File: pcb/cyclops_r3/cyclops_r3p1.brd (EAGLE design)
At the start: 69.8 x 53.3 mm, 74 parts, among them Q1 SUM11006, Q2 IRF510, U1 MCP4921, U2 317-N, U3 ADR03, U4 OP1177, U5 LM324N, U6 ZXTD45, U8 TLV3701CDBVT

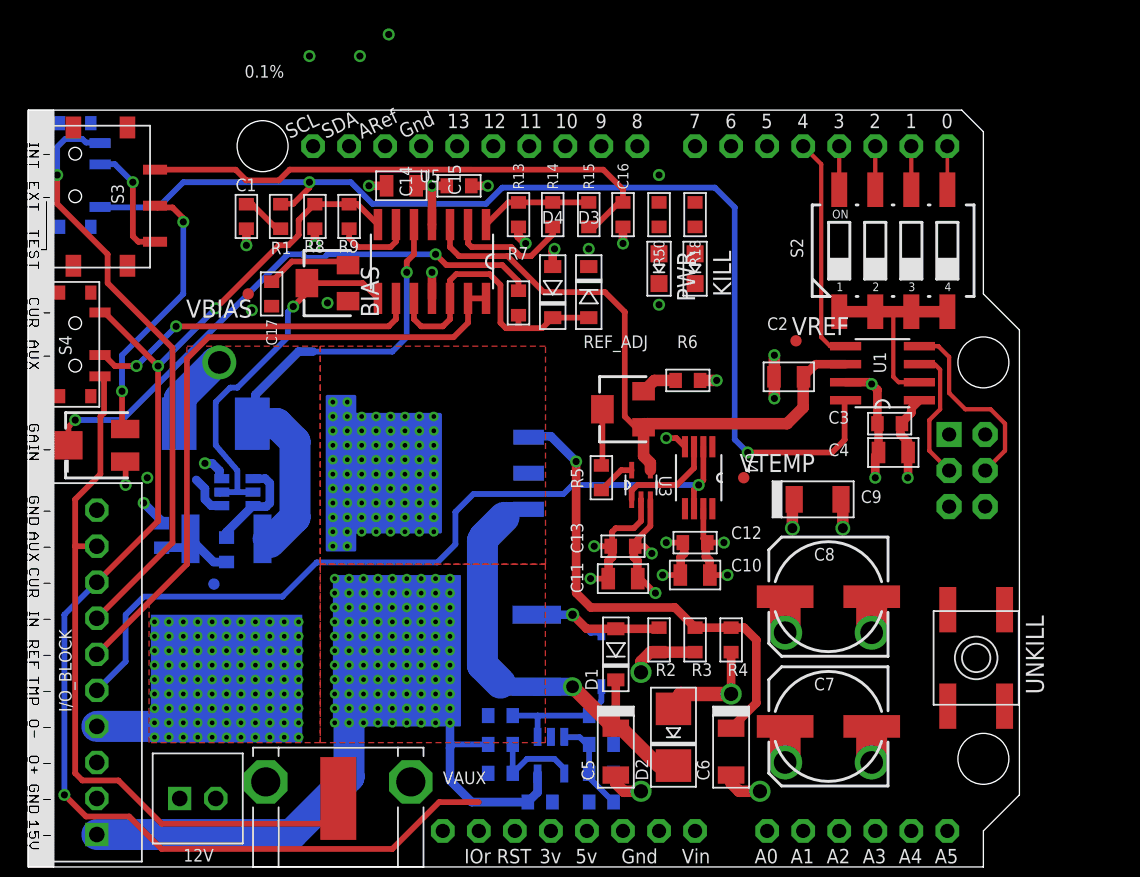
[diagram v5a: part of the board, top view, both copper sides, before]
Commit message: Several changes to board layout. Also, some new design notes.
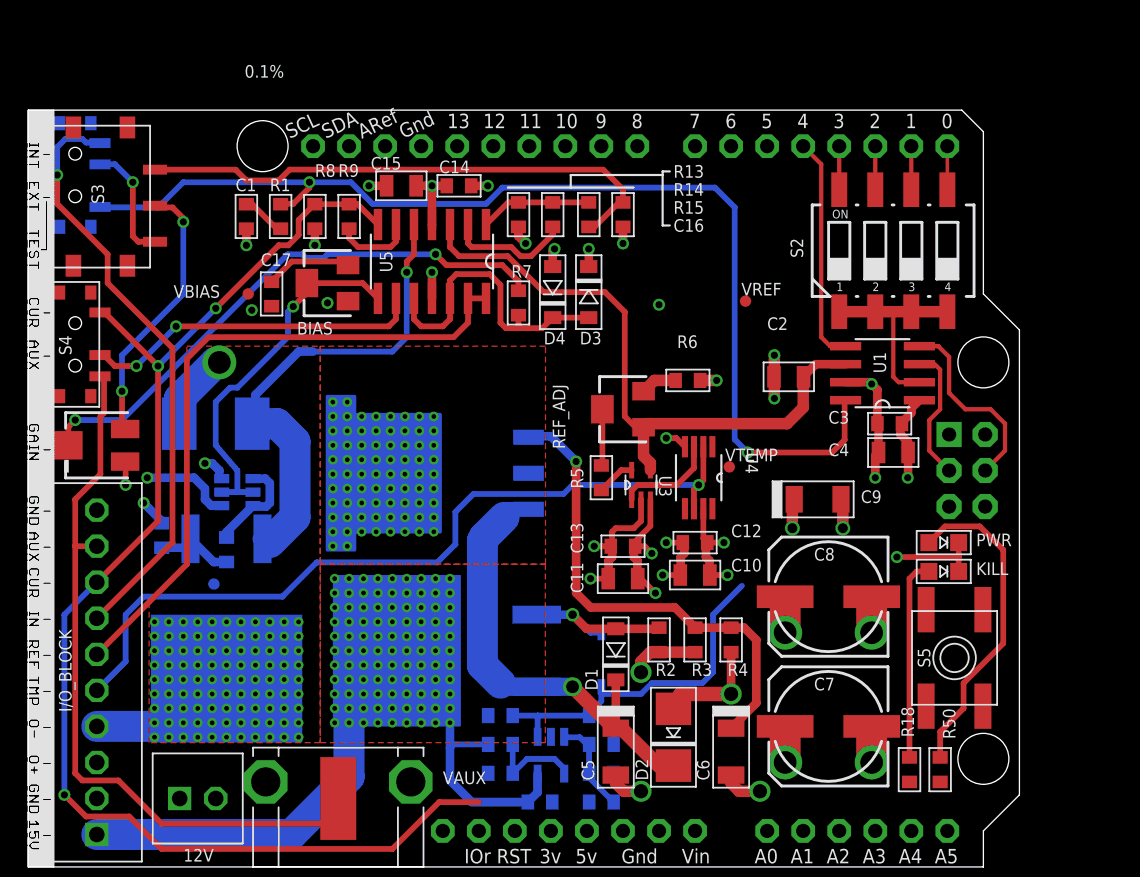
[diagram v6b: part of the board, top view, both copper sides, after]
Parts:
- removed UNKILL: SPST_TACT-EVQQ2, cyclops:EVQ-Q2
- added S5: UNKILL, cyclops:EVQ-Q2
- moved R50 43.8 mm to (63.0, 6.86), turned to 270 degrees
- moved R18 41.9 mm to (60.8, 6.86), turned to 270 degrees
- moved PWR 27.8 mm to (63.2, 22.9), turned to 270 degrees
- moved KILL 27.6 mm to (63.2, 20.8), turned to 270 degrees
- moved VREF 4.52 mm to (49.3, 39.9)
- moved VTEMP 1.27 mm to (48.1, 28.2)
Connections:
- removed net AGND: BIAS.3, C17.2, UNKILL.B, UNKILL.B'
- net COMP+: now also S5.A, S5.A'; no longer UNKILL.A, UNKILL.A'
- net GND: now also BIAS.3, C17.2, S5.B, S5.B'
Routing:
- net N$3: track 0.00 -> 22.9 mm
- net KILL: track 9.28 -> 24.7 mm
- net N$11: track 0.00 -> 14.2 mm
- net GND: track 68.7 -> 81.2 mm, vias 31 -> 30
- net AGND: track 6.08 -> 0.00 mm
- net +12V: track 40.5 -> 45.3 mm, vias 91 -> 89

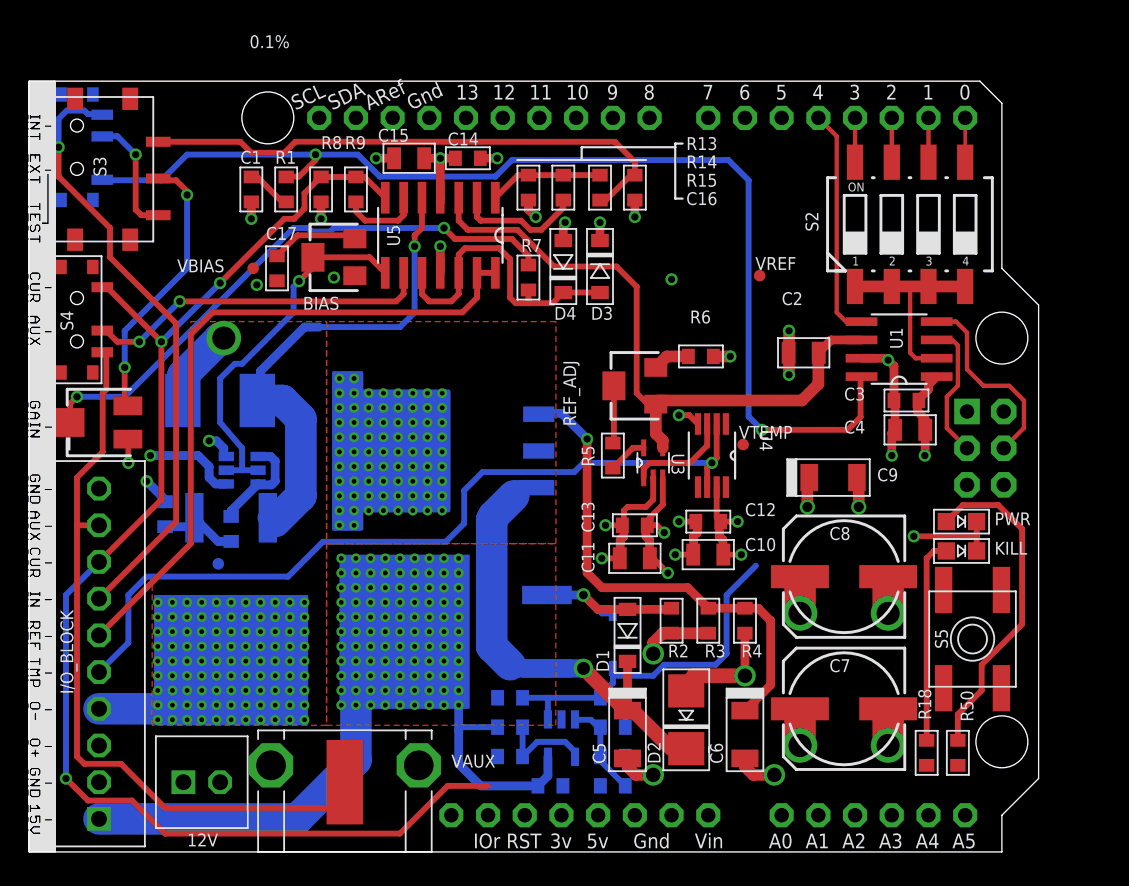
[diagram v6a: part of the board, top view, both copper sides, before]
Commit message: Added a negative rail, used exclusively by the opamp, to allow a wider bandwidth. Finished routing everything. Need to make bottom silkscreen and finish testing comparitor circuit.
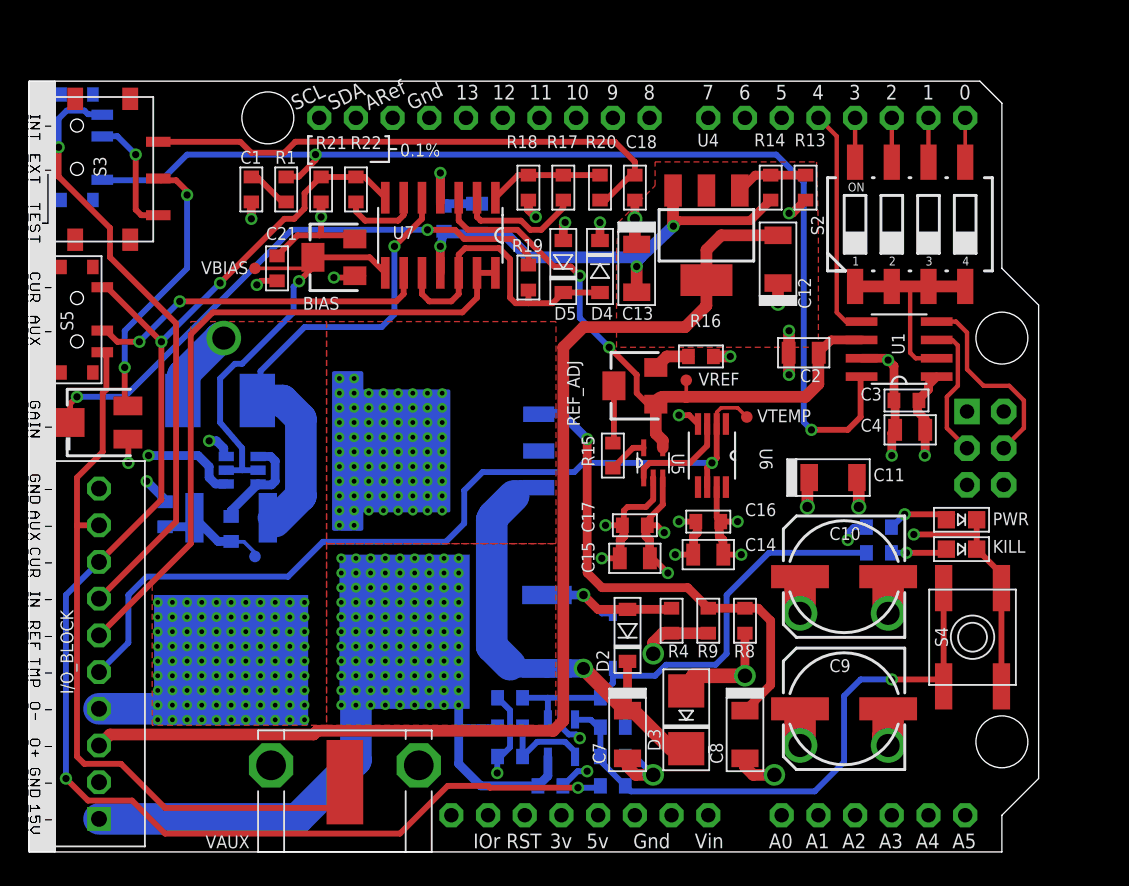
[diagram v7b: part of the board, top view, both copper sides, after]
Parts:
- removed 12V: SCREW2, cyclops:SCREW2
- removed R50: 2.4k, cyclops:0603
- added C20: 1uF, cyclops:0805
- added C21: .1uF, cyclops:0603
- added R22: 9k, cyclops:0603
- added R23: 10, cyclops:0603
- added R24: 1k, cyclops:0603
- added U7: LM324N, cyclops:SO14
- C10: value 1uF -> 47uF; device cyclops:0805 -> cyclops:153CLV-0807
- C11: device cyclops:0805 -> cyclops:1206-POL
- C12, C13: value .1uF -> 1uF; device cyclops:0603 -> cyclops:1206-POL
- C14: value .1uF -> 1uF; device cyclops:0603 -> cyclops:0805
- C19: value 10pF -> .1uF
- C5: value 1uF -> 10pF; device cyclops:1206-POL -> cyclops:0603
- C6: value 10uF -> .1uF; device cyclops:1206-POL -> cyclops:0603
- C7: value 47uF -> 1uF; device cyclops:153CLV-0807 -> cyclops:1206-POL
- C8: value 47uF -> 10uF; device cyclops:153CLV-0807 -> cyclops:1206-POL
- C9: value 1uF -> 47uF; device cyclops:1206-POL -> cyclops:153CLV-0807
- D1: value MMSZ -> (none); device cyclops:SOD123 -> cyclops:SOD-323F
- D2: value S1B -> MMSZ; device cyclops:SMA-DO214AC -> cyclops:SOD123
- D3: value DS11015 -> S1B; device cyclops:SOD123 -> cyclops:SMA-DO214AC
- D5: value (none) -> DS11015; device cyclops:SOD-323F -> cyclops:SOD123
- R10: value 10 -> 220k
- R11: value 220k -> 3.0k
- R12: value 1k -> 2.4k
- R13: value 1k -> 75
- R14: value 1k -> 120
- R15: value 1k -> 470
- R16: value 100k -> 1k
- R18: value 3.0k -> 1k
- R19: value 4k -> 1k
- R2: value 10k -> 100k
- R20: value 56k -> 1k
- R21: value 91k -> 1k
- R3: value 2.1k -> 56k
- R4: value 240 -> 10k
- R5: value 470 -> 4k
- R6: value 1k -> 91k
- R8: value 1k -> 240
- R9: value 9k -> 2.1k
- S4: value CURR/AUX -> UNKILL; device cyclops:PCM12 -> cyclops:EVQ-Q2
- S5: value UNKILL -> CURR/AUX; device cyclops:EVQ-Q2 -> cyclops:PCM12
- U2: value 317-N -> TLV37; device cyclops:TO-263 -> ti-extended:SOT95P280X145-5N
- U3: value ADR03 -> 317-N; device cyclops:SOT65P210X110-5N -> cyclops:TO-263
- U4: value OP1177 -> 337-N; device cyclops:SOP65P490X110-8N -> cyclops:SOT223
- U5: value LM324N -> ADR03; device cyclops:SO14 -> cyclops:SOT65P210X110-5N
- U6: value ZXTD45 -> OP1177; device cyclops:SOT23-6 -> cyclops:SOP65P490X110-8N
- U8: value TLV3701CDBVT -> ZXTD45; device ti-extended:SOT95P280X145-5N -> cyclops:SOT23-6
- moved S5 65.8 mm to (2.03, 36.8)
- moved S4 65.8 mm to (64.0, 14.9)
- moved R12 49.4 mm to (57.5, 22.5), turned to 0 degrees
- moved R18 47.8 mm to (33.3, 46.0)
- moved R21 42.3 mm to (18.9, 45.8), flipped to the top, turned to 270 degrees
- moved R8 41.8 mm to (48.3, 16.0)
- moved C18 41.8 mm to (40.6, 46.0), flipped to the top, turned to 270 degrees
- moved C19 39.0 mm to (27.4, 43.8), turned to 270 degrees
- moved R9 38.5 mm to (45.7, 16.0)
- moved R20 37.9 mm to (38.2, 46.0), flipped to the top, turned to 270 degrees
- moved R17 35.5 mm to (35.7, 46.0), flipped to the top, turned to 270 degrees
- moved R19 33.2 mm to (33.3, 39.8), flipped to the top, turned to 270 degrees
- moved U6 32.5 mm to (46.0, 27.4), flipped to the top, turned to 270 degrees
- moved C14 32.1 mm to (45.7, 20.6), turned to 180 degrees
- moved D3 31.9 mm to (44.2, 9.14), turned to 270 degrees
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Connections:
- new net -2.1V: C13.-, C19.2, C20.2, R14.1, U4.3, U7.11
- new net -5V: C12.-, I/O_BLOCK.P$3, U4.4
- new net N$12: R13.1, R14.2, U4.1
- net +12V: now also C10.+, C11.+, C16.1, C19.1, C20.1, C21.1, D3.A, D4.C, R12.2, R8.2, U3.2, U3.4, U5.3, U6.7, U7.4, U8.1; no longer 12V.P$2, C10.1, C11.1, C12.1, C13.1, C7.+, C8.+, D2.A, D3.C, I/O_BLOCK.P$3, R4.2, R50.2, U2.2, U2.4, U3.3, U4.7, U5.4, U6.1
- net +15V: now also C6.1, R3.1, U2.5; no longer C18.1, R20.1, U8.5
- net +15V_RECT: now also C7.+, D3.C, U3.3; no longer C5.+, D1.C, U2.3
- net COMP+: now also C5.1, R2.1, R6.2, S4.A, S4.A', U2.3; no longer C19.1, R16.1, R21.2, S5.A, S5.A', U8.3
- net GND: now also C10.-, C11.-, C12.+, C13.+, C21.2, C5.2, C6.2, D5.A, R10.1, R16.1, R18.2, R21.2, R24.1, R4.1, R5.2, R9.1, S4.B, S4.B', U2.2, U5.2, U6.4, U8.3; no longer 12V.P$1, C10.2, C11.2, C12.2, C13.2, C19.2, C5.-, C6.-, D4.A, R11.1, R12.1, R19.2, R2.1, R3.1, R6.1, R8.2, S5.B, S5.B', U3.2, U4.4, U5.11, U6.3, U8.2
- net KILL: now also D1.A, R10.2, R7.1, U2.1; no longer D5.A, R17.1, R18.2, U8.1
- net N$10: now also R23.1, U8.4, U8.6; no longer R10.1, U6.4, U6.6
- net N$11: now also R11.1; no longer R18.1
- net N$13: now also R23.2, R24.2; no longer R10.2, R12.2
- net N$15: now also R22.1, U7.6; no longer R9.1, U5.6
- net N$18: now also D1.C, D2.A, R4.2; no longer D1.A, D5.C, R2.2
- net N$2: now also U7.5; no longer U5.5
- net N$20: now also R15.2, U5.5; no longer R5.2, U3.5
- net N$22: now also R15.1; no longer R5.1
- net N$3: now also R12.1; no longer R50.1
- net N$4: now also U7.8, U8.2, U8.5; no longer U5.8, U6.2, U6.5
- net N$5: now also R3.2, R5.1, U2.4; no longer R19.1, R20.2, U8.4
- net N$6: now also R16.2; no longer R6.2
- net N$7: now also R19.1; no longer R7.1
- net N$72: now also C8.+, R8.1, R9.2, U3.1; no longer C6.+, R3.2, R4.1, U2.1
- net N$8: now also R17.2, U7.2; no longer R14.2, U5.2
- net N$9: now also R6.1, R7.2; no longer R17.2, R21.1
- net REFA: now also U5.4, U7.3; no longer U3.4, U5.3
- net REFA2X: now also C18.1, R20.2; no longer C16.1, R15.2
- net TEMP: now also U5.1, U6.3; no longer U3.1, U4.3
- net VAUX: now also S5.3; no longer S4.3
- net VFB: now also S5.2, U7.9; no longer S4.2, U5.9
- net VI: now also R2.2, R21.1, R22.2, S5.1, U7.7; no longer R16.2, R8.1, R9.2, S4.1, U5.7
- net VREF: now also U7.13, U7.14; no longer U5.13, U5.14
- net VREFA2X: now also R17.1, R18.1, R20.1, U7.1; no longer R13.1, R14.1, R15.1, U5.1
- net VTEMP: now also U6.2, U6.6; no longer U4.2, U4.6
- net _VREF: now also D4.A, D5.C, R19.2, U7.10, U7.12; no longer D3.A, D4.C, R7.2, U5.10, U5.12
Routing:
- net -5V: track 0.00 -> 79.0 mm
- net COMP+: track 6.77 -> 41.8 mm, vias 0 -> 1
- net -2.1V: track 0.00 -> 33.8 mm, vias 0 -> 3
- net GND: track 81.2 -> 106.8 mm, vias 30 -> 31
- net N$3: track 22.9 -> 5.12 mm, vias 0 -> 1
- net N$11: track 14.2 -> 4.02 mm, vias 0 -> 1
- net KILL: track 24.7 -> 32.7 mm
- net +12V: track 45.3 -> 53.2 mm, vias 89 -> 90
- net VI: track 92.2 -> 100.1 mm, vias 3 -> 4
- net N$12: track 0.00 -> 4.99 mm
- net N$4: track 26.0 -> 30.1 mm
- net VTEMP: track 56.3 -> 59.6 mm
- net N$13: track 5.81 -> 8.04 mm
- net DACA: track 77.8 -> 77.0 mm
- net N$2: track 34.8 -> 34.1 mm
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- added copper zone on layer 1, net -5V
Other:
- board text removed: "CYCLOPS R3.1 | ---------- Designed by: Jon Newman | --------------------- Manual: www.jonnewman.net/cyclops3 | ------------------------------ Open-source electronics License: CC BY-SA 4.0 | -------------------"
